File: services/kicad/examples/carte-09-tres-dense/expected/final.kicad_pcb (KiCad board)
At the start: 2 copper layers, 130 x 100 mm, 62 parts, among them J1 IN_5V, J10 IO0, J11 IO1, J12 IO2, J13 IO3, J14 IO4, J2 SWD, U1 STM32F103C8T6, U2 AMS1117-3.3

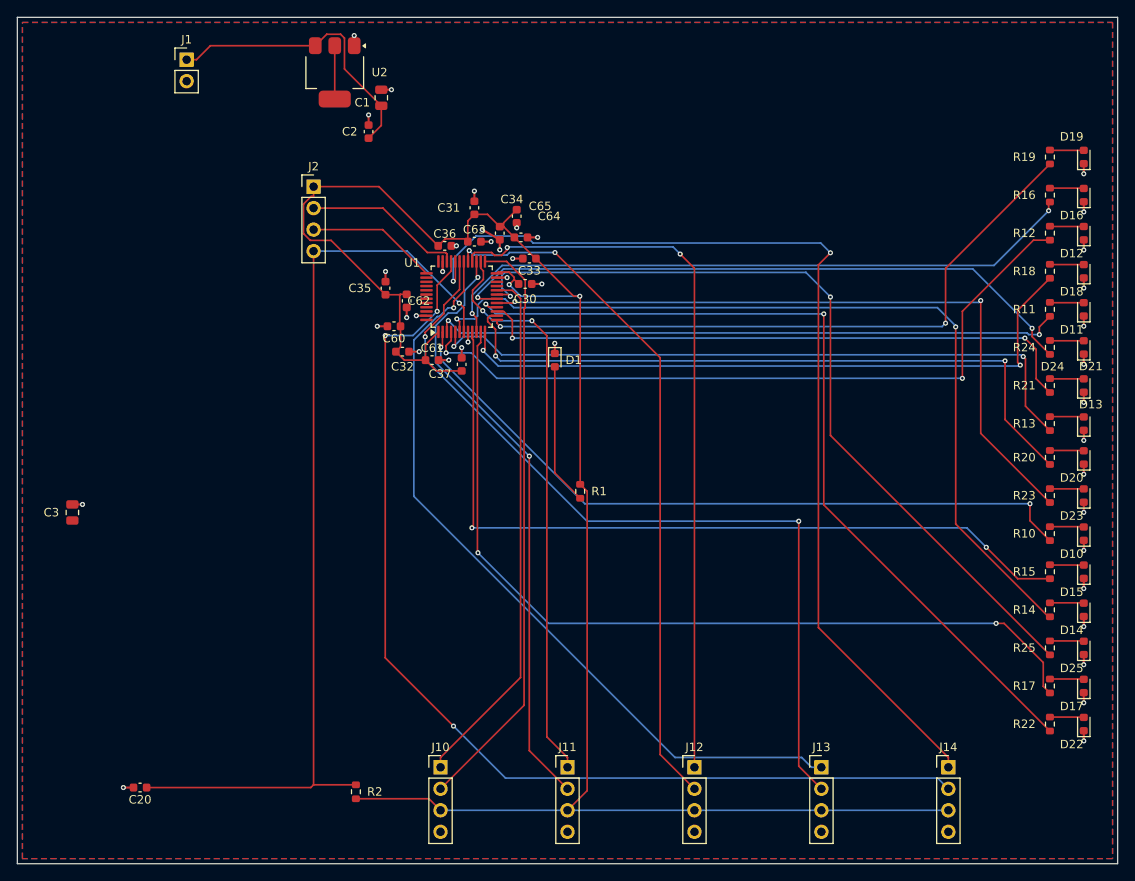
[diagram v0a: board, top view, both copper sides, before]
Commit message: fix(banc): le contour n etait JAMAIS resserre — dix cartes divisees par 2 a 4
Question de l utilisateur devant les rendus : « tu es satisfait de ce
placement ? ». Non, et la mesure lui donnait raison.

    carte-10 livree     140 x 105 mm = 14725 mm2
    son circuit          51 x  66 mm =  3366 mm2
    OCCUPATION                            23 %
    connecteurs                      56 a 75 mm du circuit
    fil de signal                      1230 mm  (VIN a lui seul 112 mm)

LA CAUSE : `run_pipeline.py` n envoyait pas `auto_size_board` a `/place/auto`.
Le resserrement du contour sur le placement existe depuis le 2026-09-13 et ne
s execute que si l appelant l autorise ; le defaut du modele est `False`.

C est le SEPTIEME levier de ce projet qui existe et que personne n appelle,
apres max_distance_mm, anchor_pin, WorkflowConfig.grid, constraints,
move_reference, bottom_up_placement et LocalRerouter.

⚠️ Et il etait INVISIBLE : la chaine de PRODUCTION passe bien le drapeau depuis
`handlePlacement`. Le banc mesurait donc un comportement que le produit n a
pas — l inverse exact de ce a quoi sert un banc.

MESURE APRES CORRECTION, meme circuit, meme graine :

    carte             demandee      REELLE        err  manq
    carte-01           25 x 20     20,1 x 14,6     0    0
    carte-02           55 x 40     34,9 x 25,4     0    0
    carte-03           50 x 35     26,1 x 20,1     0    0
    carte-04           60 x 45     36,6 x 27,2     0    0
    carte-05           70 x 50     43,6 x 32,6     0    0
    carte-06           80 x 60     48,5 x 36,4     0    0
    carte-07          110 x 80     53,2 x 38,8     0    0
    carte-08          125 x 95     56,4 x 44,1     0    0
    carte-09          130 x 100    57,3 x 45,2     0    0
    carte-10          140 x 105    61,0 x 45,8     0    0

Dix sur dix, 100 % route, aucune erreur, aucune connexion manquante. Sur
carte-10 : occupation 23 -> 56 %, fil de signal 1230 -> 652 mm, VIN 112 -> 45,5,
connecteurs 56-75 -> 23-35 mm.

ET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
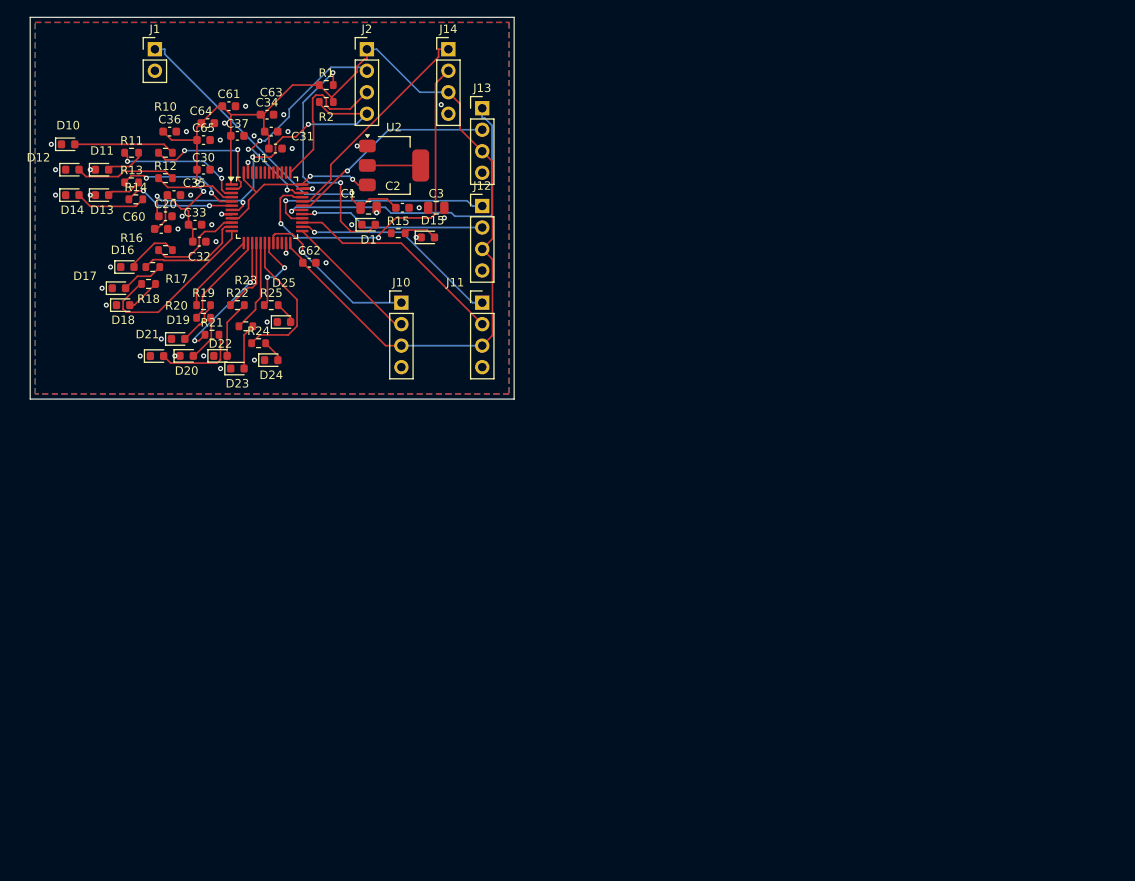
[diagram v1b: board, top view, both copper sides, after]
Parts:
- moved D14 129.2 mm to (90.0, 76.0), turned to 0 degrees
- moved D10 128.5 mm to (89.5, 70.0), turned to 0 degrees
- moved D17 123.3 mm to (95.5, 87.0), turned to 0 degrees
- moved D12 119.7 mm to (90.0, 73.0), turned to 0 degrees
- moved D13 119.1 mm to (93.5, 76.0), turned to 0 degrees
- moved R14 118.4 mm to (97.5, 76.5), turned to 0 degrees
- moved D11 117.2 mm to (93.5, 73.0), turned to 0 degrees
- moved R17 117.0 mm to (99.5, 84.5), turned to 0 degrees
- moved R10 113.8 mm to (101.0, 71.0), turned to 0 degrees
- moved D18 113.6 mm to (96.0, 89.0), turned to 0 degrees
- moved D16 113.3 mm to (96.5, 84.5), turned to 0 degrees
- moved R13 112.2 mm to (97.0, 74.5), turned to 0 degrees
- moved D22 110.9 mm to (107.5, 95.0), turned to 0 degrees
- moved R11 110.1 mm to (97.0, 71.0), turned to 0 degrees
- moved D21 109.6 mm to (100.0, 95.0), turned to 0 degrees
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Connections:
- U1 pad 36: Net-(U1-36) -> PWR_FLAG
- U1 pad 48: Net-(U1-48) -> PWR_FLAG
- U1 pad 9: IO_L5 -> PWR_FLAG
- U2 pad 3: VIN -> PWR_FLAG
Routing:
- net IO_L5: track 94.1 -> 0.00 mm, vias 2 -> 0
- net IO_L12: track 102.2 -> 8.93 mm, vias 2 -> 0
- net EXT4_1: track 119.3 -> 26.3 mm, vias 2 -> 0
- net +3V3: track 231.0 -> 140.9 mm
- net IO_L4: track 102.8 -> 13.3 mm
- net IO_L7: track 102.4 -> 13.1 mm, vias 2 -> 0
- net IO_L15: track 97.7 -> 9.63 mm
- net EXT4_2: track 124.9 -> 43.6 mm, vias 3 -> 2
- net IO_L2: track 86.7 -> 9.71 mm, vias 2 -> 0
- net IO_L13: track 84.6 -> 10.9 mm, vias 2 -> 0
- net EXT3_2: track 98.0 -> 25.0 mm, vias 2 -> 1
- net IO_L10: track 81.0 -> 11.4 mm, vias 2 -> 0
- net IO_L0: track 85.4 -> 16.0 mm
- net NRST: track 111.3 -> 43.1 mm, vias 1 -> 4
- net IO_L9: track 77.6 -> 9.65 mm, vias 2 -> 0
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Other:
- board size 130 x 100 mm -> 57.2 x 45.1 mm

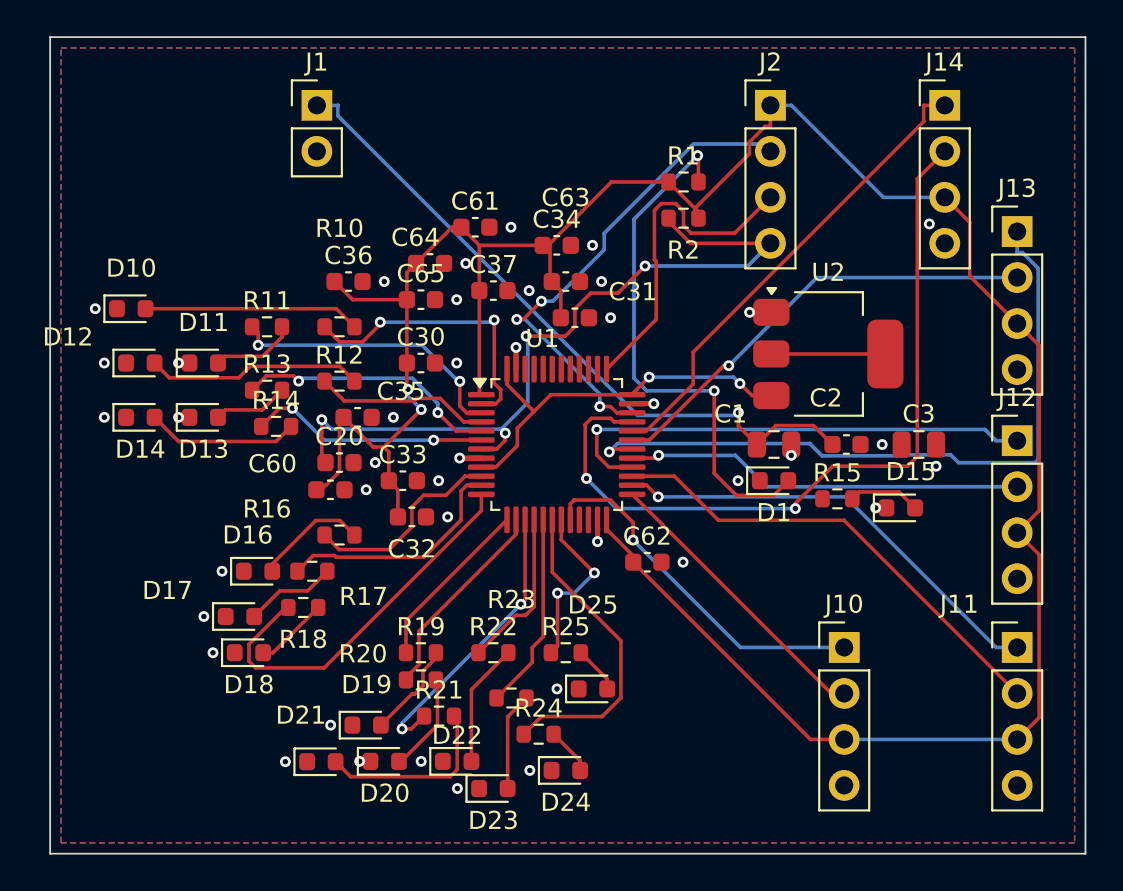
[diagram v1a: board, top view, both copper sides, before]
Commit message: feat(placement): les peripheriques se REPARTISSENT, ils ne s empilent plus
Question de l utilisateur devant le rendu : « c est quoi ce type de placement ? ».
Les composants s entassaient d un seul cote du boitier, etiquettes de
serigraphie l une sur l autre, trois quarts de la couronne vides.

TROIS CAUSES, toutes dans `_poser_les_peripheriques`, toutes la meme faute —
un angle unique pour tout un groupe :

  - les DIRECTS qui visent la meme broche (tous les decouplages d un rail,
    toutes les resistances d un meme signal) recevaient le MEME `angle_vers`
    et le meme rayon de depart ;
  - les SUIVEURS d un meme parent recevaient tous atan2(parent - centre) ;
  - les ISOLES partaient tous de l angle 0.0, c est-a-dire du meme point.

`le_long_du_rayon` ne s ecartait qu une fois la place prise : d ou la file.

REMEDE : `_ecart_en_eventail`. Le PREMIER de chaque groupe garde EXACTEMENT la
direction calculee — c est la topologie, on ne la perd pas pour faire joli — et
les suivants s ecartent symetriquement de 3 x `_PAS_ANGLE_DEG`.
Rien de deja pose ne bouge : seul l ANGLE DE DEPART de la recherche change, et
`le_long_du_rayon` reste seul juge de ce qui est libre.

BANC DES DIX CARTES, contour resserre ET peripheriques repartis :

    carte             demandee    livree         err  manq
    carte-01           25 x 20    20,1 x 13,6     0    0
    carte-02           55 x 40    34,9 x 25,2     0    0
    carte-03           50 x 35    27,6 x 19,9     0    0
    carte-04           60 x 45    36,6 x 29,8     0    0
    carte-05           70 x 50    40,0 x 32,6     0    0
    carte-06           80 x 60    46,5 x 36,4     0    0
    carte-07          110 x 80    47,7 x 38,8     0    0
    carte-08          125 x 95    57,4 x 44,1     0    0
    carte-09          130 x 100   57,8 x 45,2     0    0
    carte-10          140 x 105   59,0 x 45,8     0    0

Dix sur dix, 100 % route. carte-07 gagne 5,5 mm de largeur sur le passage
precedent, carte-06 deux, carte-10 deux. Sur ca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
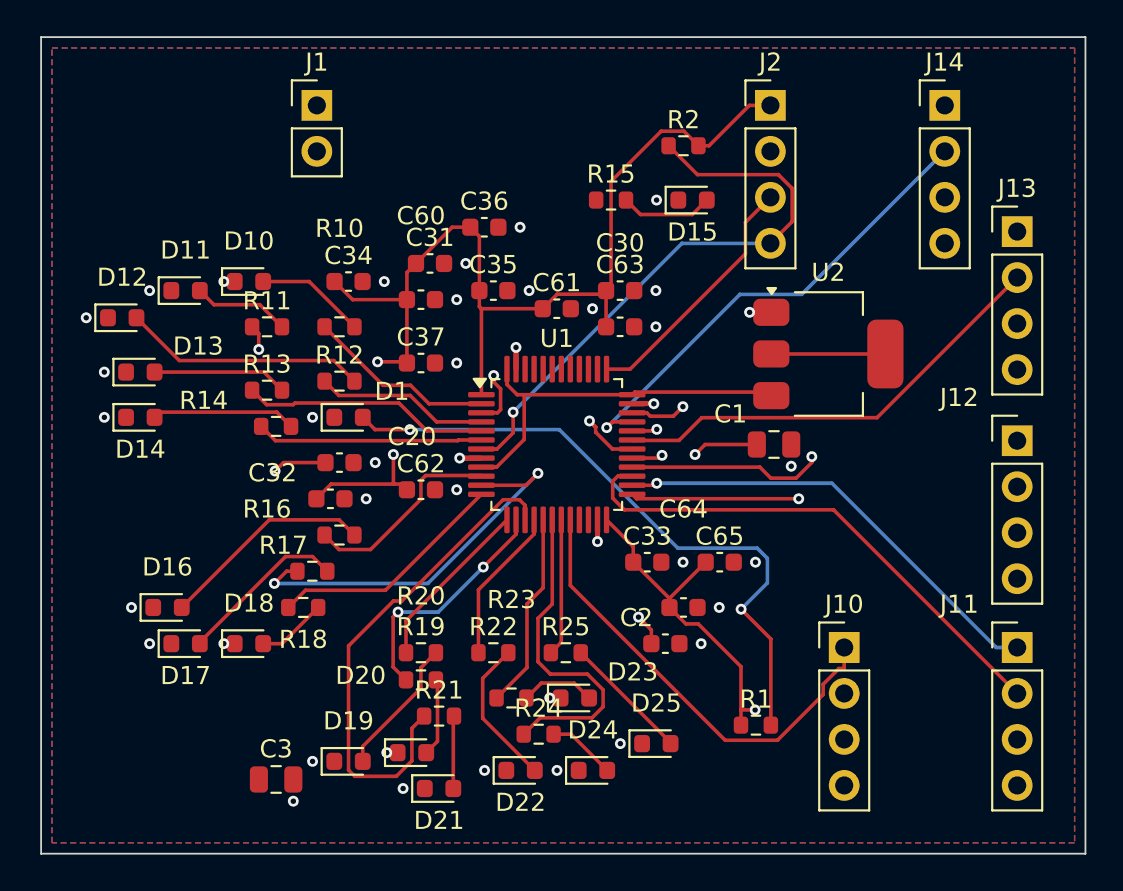
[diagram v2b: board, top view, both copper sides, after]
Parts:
- moved C3 40.0 mm to (97.5, 96.0)
- moved R1 30.3 mm to (124.0, 93.0)
- moved D1 23.8 mm to (101.5, 76.0)
- moved C64 23.6 mm to (120.0, 86.5)
- moved C65 22.0 mm to (122.0, 84.0)
- moved R15 20.7 mm to (116.0, 64.0)
- moved D15 20.5 mm to (120.5, 64.0)
- moved C2 14.9 mm to (119.0, 88.5)
- moved C33 14.2 mm to (118.0, 84.0)
- moved C62 13.1 mm to (105.5, 80.0)
- moved C34 11.7 mm to (101.5, 68.5)
- moved C60 11.6 mm to (105.5, 69.5)
- moved C30 11.2 mm to (116.5, 71.0)
- moved C35 10.3 mm to (109.5, 69.0)
- moved C31 8.54 mm to (106.0, 67.5)
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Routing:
- net EXT4_2: track 43.6 -> 26.5 mm, vias 2 -> 1
- net VIN: track 38.0 -> 49.9 mm, vias 1 -> 2
- net IO_L11: track 15.9 -> 27.6 mm, vias 2 -> 0
- net IO_L7: track 13.1 -> 22.0 mm, vias 0 -> 2
- net SWDIO: track 27.6 -> 19.2 mm, vias 3 -> 1
- net IO_L8: track 21.4 -> 13.3 mm
- net NRST: track 43.1 -> 50.1 mm, vias 4 -> 2
- net EXT3_1: track 39.0 -> 32.2 mm
- net LED_PWR: track 29.4 -> 36.1 mm
- net LEDA11: track 10.2 -> 4.02 mm
- net LEDA0: track 12.0 -> 6.07 mm
- net LEDA6: track 6.26 -> 11.9 mm
- net IO_L0: track 16.0 -> 10.4 mm, vias 2 -> 0
- net EXT0_1: track 20.0 -> 25.4 mm, vias 1 -> 0
- net EXT0_2: track 16.3 -> 21.1 mm, vias 0 -> 1
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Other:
- board size 57.2 x 45.1 mm -> 57.7 x 45.1 mm
- copper layers 2 -> 4

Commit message: docs(banc): les dix boards du banc du 2026-09-23, service corrige
Artefacts du banc dont le tableau est deja commite : les dix cartes a
100 % route, 0 erreur, 0 connexion manquante, chacune a la taille de son
circuit.

Co-Authored-By: Claude Opus 5 <noreply@anthropic.com>
Claude-Session: https://claude.ai/code/session_01TnMqm4La2CxQHHB5K8aSSV
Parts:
- moved C36 15.0 mm to (105.0, 80.0)
- moved C34 14.1 mm to (105.5, 82.0)
- moved C63 13.2 mm to (103.5, 67.0)
- moved C32 11.5 mm to (101.0, 69.0)
- moved C31 10.6 mm to (116.0, 71.0)
- moved C62 10.5 mm to (105.5, 69.5)
- moved C64 9.51 mm to (110.5, 86.0)
- moved C30 3.64 mm to (113.0, 70.0)
- moved C60 3.64 mm to (109.0, 68.5)
- moved C65 3.20 mm to (120.0, 86.5)
- moved C35 3.04 mm to (110.0, 66.0)
- moved C61 2.06 mm to (112.5, 68.0)
- moved J12 1.00 mm to (138.4, 76.3)
- moved J13 1.00 mm to (138.4, 64.7)
- moved J11 0.87 mm to (138.4, 87.8)
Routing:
- net IO_L13: track 10.9 -> 39.0 mm, vias 0 -> 2
- net NRST: track 50.1 -> 65.3 mm
- net IO_L7: track 22.0 -> 13.9 mm, vias 2 -> 0
- net EXT0_1: track 25.4 -> 19.3 mm, vias 0 -> 1
- net EXT3_1: track 32.2 -> 37.3 mm
- net EXT0_2: track 21.1 -> 16.3 mm
- net EXT2_1: track 22.6 -> 27.0 mm
- net +3V3: track 143.1 -> 146.9 mm
- net EXT4_2: track 26.5 -> 29.6 mm, vias 1 -> 2
- net IO_L14: track 18.4 -> 15.8 mm
- net VIN: track 49.9 -> 52.5 mm, vias 2 -> 1
- net IO_L8: track 13.3 -> 15.7 mm, vias 0 -> 2
- net IO_L1: track 18.2 -> 16.0 mm
- net IO_L6: track 11.3 -> 10.0 mm
- net IO_L10: track 13.2 -> 14.4 mm, vias 2 -> 0
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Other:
- copper layers 4 -> 2
